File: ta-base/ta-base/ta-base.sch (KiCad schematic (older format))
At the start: 17 parts, among them J1 PinSocket_16_base, J2 PinSocket_4_base, J3 PinSocket_5_base, J4 PinSocket_4_base, J5 PinSocket_5_base, J6 PinSocket_16_base, J7 PinSocket_5_base, J8 PinSocket_5_base, P1 Gnd_Screws, P2 Gnd_standoffs, SW1 SW_SPDT, SW2 SW_SPDT, U1 BSB008NE2LXXUMA1, U2 burn_wire

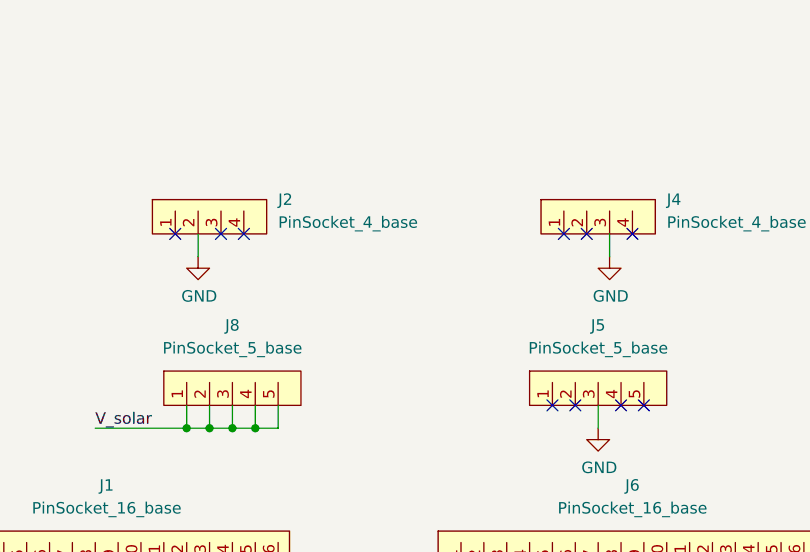
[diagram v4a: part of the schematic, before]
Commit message: fixed gnd bug on base plate
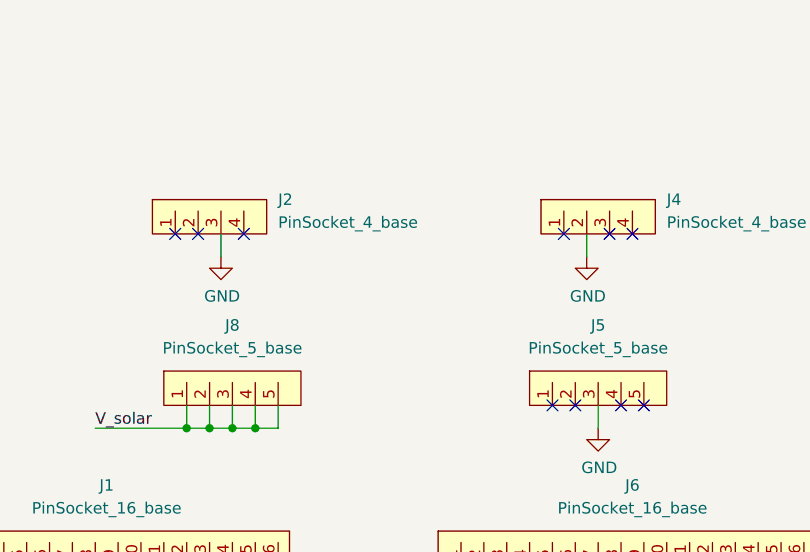
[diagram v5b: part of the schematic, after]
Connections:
- net GND: now also J2.3, J4.2; no longer J2.2, J4.3
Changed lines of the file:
@@
 Sheet 1 1
 Title "Tartan Artibeus Base Plate"
-Date ""
+Date "2021-08-25"
 Rev "v0"
 Comp "Carnegie Mellon University-- Abstract Research Group"
@@
 NoConn ~ 3100 4050
 $Comp
-L ta-base:PinSocket_4_base J2
-U 1 1 60FCFD38
-P 8000 1950
-F 0 "J2" H 8300 2100 50  0000 L CNN
-F 1 "PinSocket_4_base" H 8300 2000 50  0000 L CNN
-F 2 "ta-base:PinSocket_1x4_TartanArtibeus_base_cpy" H 7950 1950 50  0001 C CNN
-F 3 "" H 7950 1950 50  0001 C CNN
-	1    8000 1950
-	1    0    0    -1
-$EndComp
-$Comp
 L ta-base:PinSocket_4_base J4
 U 1 1 60FD0B5F
@@
 	6900 3600 6400 3600
 NoConn ~ 7850 1950
-NoConn ~ 8050 1950
 NoConn ~ 8150 1950
 Text Label 6450 3500 0    50   ~ 0
@@
 L power:GND #PWR07
 U 1 1 60FB439D
-P 7950 2050
-F 0 "#PWR07" H 7950 1800 50  0001 C CNN
-F 1 "GND" H 7955 1877 50  0000 C CNN
-F 2 "" H 7950 2050 50  0001 C CNN
-F 3 "" H 7950 2050 50  0001 C CNN
-	1    7950 2050
-	1    0    0    -1
-$EndComp
-Wire Wire Line
-	7950 1950 7950 2050
+P 8050 2050
+F 0 "#PWR07" H 8050 1800 50  0001 C CNN
+F 1 "GND" H 8055 1877 50  0000 C CNN
+F 2 "" H 8050 2050 50  0001 C CNN
+F 3 "" H 8050 2050 50  0001 C CNN
+	1    8050 2050
+	1    0    0    -1
+$EndComp
+Wire Wire Line
+	8050 1950 8050 2050
 Text Label 6400 3600 0    50   ~ 0
 BURN_SIG
@@
 L power:GND #PWR09
 U 1 1 60FDB343
-P 9750 2050
-F 0 "#PWR09" H 9750 1800 50  0001 C CNN
-F 1 "GND" H 9755 1877 50  0000 C CNN
-F 2 "" H 9750 2050 50  0001 C CNN
-F 3 "" H 9750 2050 50  0001 C CNN
-	1    9750 2050
-	1    0    0    -1
-$EndComp
-Wire Wire Line
-	9750 1950 9750 2050
+P 9650 2050
+F 0 "#PWR09" H 9650 1800 50  0001 C CNN
+F 1 "GND" H 9655 1877 50  0000 C CNN
+F 2 "" H 9650 2050 50  0001 C CNN
+F 3 "" H 9650 2050 50  0001 C CNN
+	1    9650 2050
+	1    0    0    -1
+$EndComp
 NoConn ~ 9550 1950
-NoConn ~ 9650 1950
 NoConn ~ 9850 1950
 NoConn ~ 9900 2700
@@
 	1    0    0    -1
 $EndComp
+$Comp
+L ta-base:PinSocket_4_base J2
+U 1 1 60FCFD38
+P 8000 1950
+F 0 "J2" H 8300 2100 50  0000 L CNN
+F 1 "PinSocket_4_base" H 8300 2000 50  0000 L CNN
+F 2 "ta-base:PinSocket_1x4_TartanArtibeus_base_cpy" H 7950 1950 50  0001 C CNN
+F 3 "" H 7950 1950 50  0001 C CNN
+	1    8000 1950
+	1    0    0    -1
+$EndComp
+NoConn ~ 7950 1950
+Wire Wire Line
+	9650 1950 9650 2050
+NoConn ~ 9750 1950
 $EndSCHEMATC
